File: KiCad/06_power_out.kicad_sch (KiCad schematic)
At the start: 20 parts, among them J601 Conn_02x03_Odd_Even, J602 Conn_02x03_Odd_Even

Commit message: Fill BOM table
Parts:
- C601, C602, C603: footprint Capacitor_SMD:C_0805_2012Metric -> Capacitor_SMD:C_0603_1608Metric; Manufacturer Part Number (none) -> CL10A226MP8NUNE; Manufacturer Product Number CL21A226MQQNNNE -> (none)
- S601, S602, S603: Manufacturer (none) -> XKB Connectivity; Manufacturer Part Number (none) -> XKB5858-Z; Manufacturer_Name XKB Connectivity -> (none); Manufacturer_Part_Number XKB5858-Z -> (none)
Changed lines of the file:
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@@
 			)
 		)
-		(property "Footprint" "Capacitor_SMD:C_0805_2012Metric"
+		(property "Footprint" "Capacitor_SMD:C_0603_1608Metric"
 			(at 116.5352 129.54 0)
 			(effects
@@
 			)
 		)
-		(property "Manufacturer Product Number" "CL21A226MQQNNNE"
+		(property "Manufacturer Part Number" "CL10A226MP8NUNE"
 			(at 115.57 125.73 0)
 			(effects
@@
 			)
 		)
-		(property "Manufacturer_Name" "XKB Connectivity"
-			(at 80.01 539.37 0)
-			(effects
-				(font
-					(size 1.27 1.27)
-				)
-				(justify left top)
-				(hide yes)
-			)
-		)
-		(property "Manufacturer_Part_Number" "XKB5858-Z"
-			(at 80.01 639.37 0)
+		(property "Arrow Part Number" ""
+			(at 80.01 939.37 0)
 			(effects
 				(font
@@
 			)
 		)
-		(property "Mouser Part Number" ""
-			(at 80.01 739.37 0)
+		(property "Arrow Price/Stock" ""
+			(at 80.01 1039.37 0)
 			(effects
 				(font
@@
 			)
 		)
-		(property "Mouser Price/Stock" ""
-			(at 80.01 839.37 0)
+		(property "Manufacturer" "XKB Connectivity"
+			(at 53.34 44.45 0)
 			(effects
 				(font
 					(size 1.27 1.27)
 				)
-				(justify left top)
 				(hide yes)
 			)
 		)
-		(property "Arrow Part Number" ""
-			(at 80.01 939.37 0)
+		(property "Manufacturer Part Number" "XKB5858-Z"
+			(at 53.34 44.45 0)
 			(effects
 				(font
 					(size 1.27 1.27)
 				)
-				(justify left top)
-				(hide yes)
-			)
-		)
-		(property "Arrow Price/Stock" ""
-			(at 80.01 1039.37 0)
-			(effects
-				(font
-					(size 1.27 1.27)
-				)
-				(justify left top)
 				(hide yes)
 			)
@@
 			)
 		)
-		(property "Footprint" "Capacitor_SMD:C_0805_2012Metric"
+		(property "Footprint" "Capacitor_SMD:C_0603_1608Metric"
 			(at 112.7252 48.26 0)
 			(effects
@@
 			)
 		)
-		(property "Manufacturer Product Number" "CL21A226MQQNNNE"
+		(property "Manufacturer Part Number" "CL10A226MP8NUNE"
 			(at 111.76 44.45 0)
 			(effects
@@
 			)
 		)
-		(property "Manufacturer_Name" "XKB Connectivity"
-			(at 80.01 618.11 0)
-			(effects
-				(font
-					(size 1.27 1.27)
-				)
-				(justify left top)
-				(hide yes)
-			)
-		)
-		(property "Manufacturer_Part_Number" "XKB5858-Z"
-			(at 80.01 718.11 0)
-			(effects
-				(font
-					(size 1.27 1.27)
-				)
-				(justify left top)
-				(hide yes)
-			)
-		)
-		(property "Mouser Part Number" ""
-			(at 80.01 818.11 0)
+		(property "Arrow Part Number" ""
+			(at 80.01 1018.11 0)
 			(effects
 				(font
@@
 			)
 		)
-		(property "Mouser Price/Stock" ""
-			(at 80.01 918.11 0)
+		(property "Arrow Price/Stock" ""
+			(at 80.01 1118.11 0)
 			(effects
 				(font
@@
 			)
 		)
-		(property "Arrow Part Number" ""
-			(at 80.01 1018.11 0)
+		(property "Manufacturer" "XKB Connectivity"
+			(at 53.34 123.19 0)
 			(effects
 				(font
 					(size 1.27 1.27)
 				)
-				(justify left top)
 				(hide yes)
 			)
 		)
-		(property "Arrow Price/Stock" ""
-			(at 80.01 1118.11 0)
+		(property "Manufacturer Part Number" "XKB5858-Z"
+			(at 53.34 123.19 0)
 			(effects
 				(font
 					(size 1.27 1.27)
 				)
-				(justify left top)
 				(hide yes)
 			)
@@
 			)
 		)
-		(property "Manufacturer_Name" "XKB Connectivity"
-			(at 80.01 577.47 0)
-			(effects
-				(font
-					(size 1.27 1.27)
-				)
-				(justify left top)
-				(hide yes)
-			)
-		)
-		(property "Manufacturer_Part_Number" "XKB5858-Z"
-			(at 80.01 677.47 0)
-			(effects
-				(font
-					(size 1.27 1.27)
-				)
-				(justify left top)
-				(hide yes)
-			)
-		)
-		(property "Mouser Part Number" ""
-			(at 80.01 777.47 0)
+		(property "Arrow Part Number" ""
+			(at 80.01 977.47 0)
 			(effects
 				(font
@@
 			)
 		)
-		(property "Mouser Price/Stock" ""
-			(at 80.01 877.47 0)
+		(property "Arrow Price/Stock" ""
+			(at 80.01 1077.47 0)
 			(effects
 				(font
@@
 			)
 		)
-		(property "Arrow Part Number" ""
-			(at 80.01 977.47 0)
+		(property "Manufacturer" "XKB Connectivity"
+			(at 53.34 82.55 0)
 			(effects
 				(font
 					(size 1.27 1.27)
 				)
-				(justify left top)
 				(hide yes)
 			)
 		)
-		(property "Arrow Price/Stock" ""
-			(at 80.01 1077.47 0)
+		(property "Manufacturer Part Number" "XKB5858-Z"
+			(at 53.34 82.55 0)
 			(effects
 				(font
 					(size 1.27 1.27)
 				)
-				(justify left top)
 				(hide yes)
 			)
@@
 			)
 		)
-		(property "Footprint" "Capacitor_SMD:C_0805_2012Metric"
+		(property "Footprint" "Capacitor_SMD:C_0603_1608Metric"
 			(at 112.7252 86.36 0)
 			(effects
@@
 			)
 		)
-		(property "Manufacturer Product Number" "CL21A226MQQNNNE"
+		(property "Manufacturer Part Number" "CL10A226MP8NUNE"
 			(at 111.76 82.55 0)
 			(effects

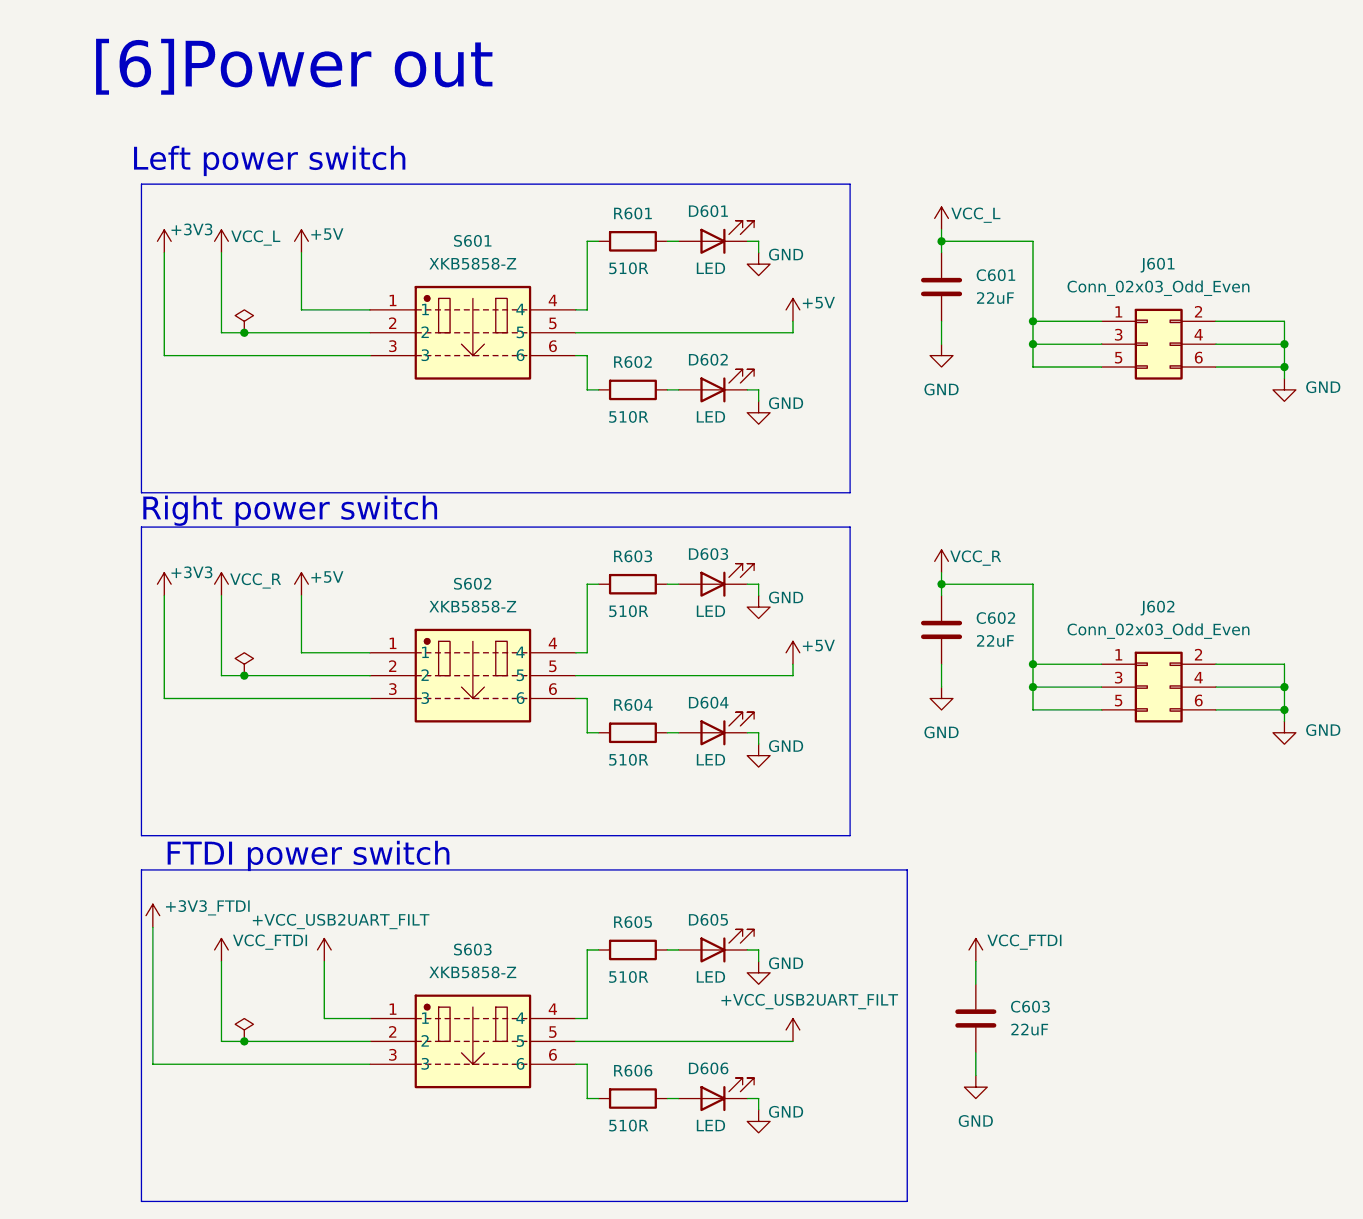
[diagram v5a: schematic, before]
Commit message: Update battery connector
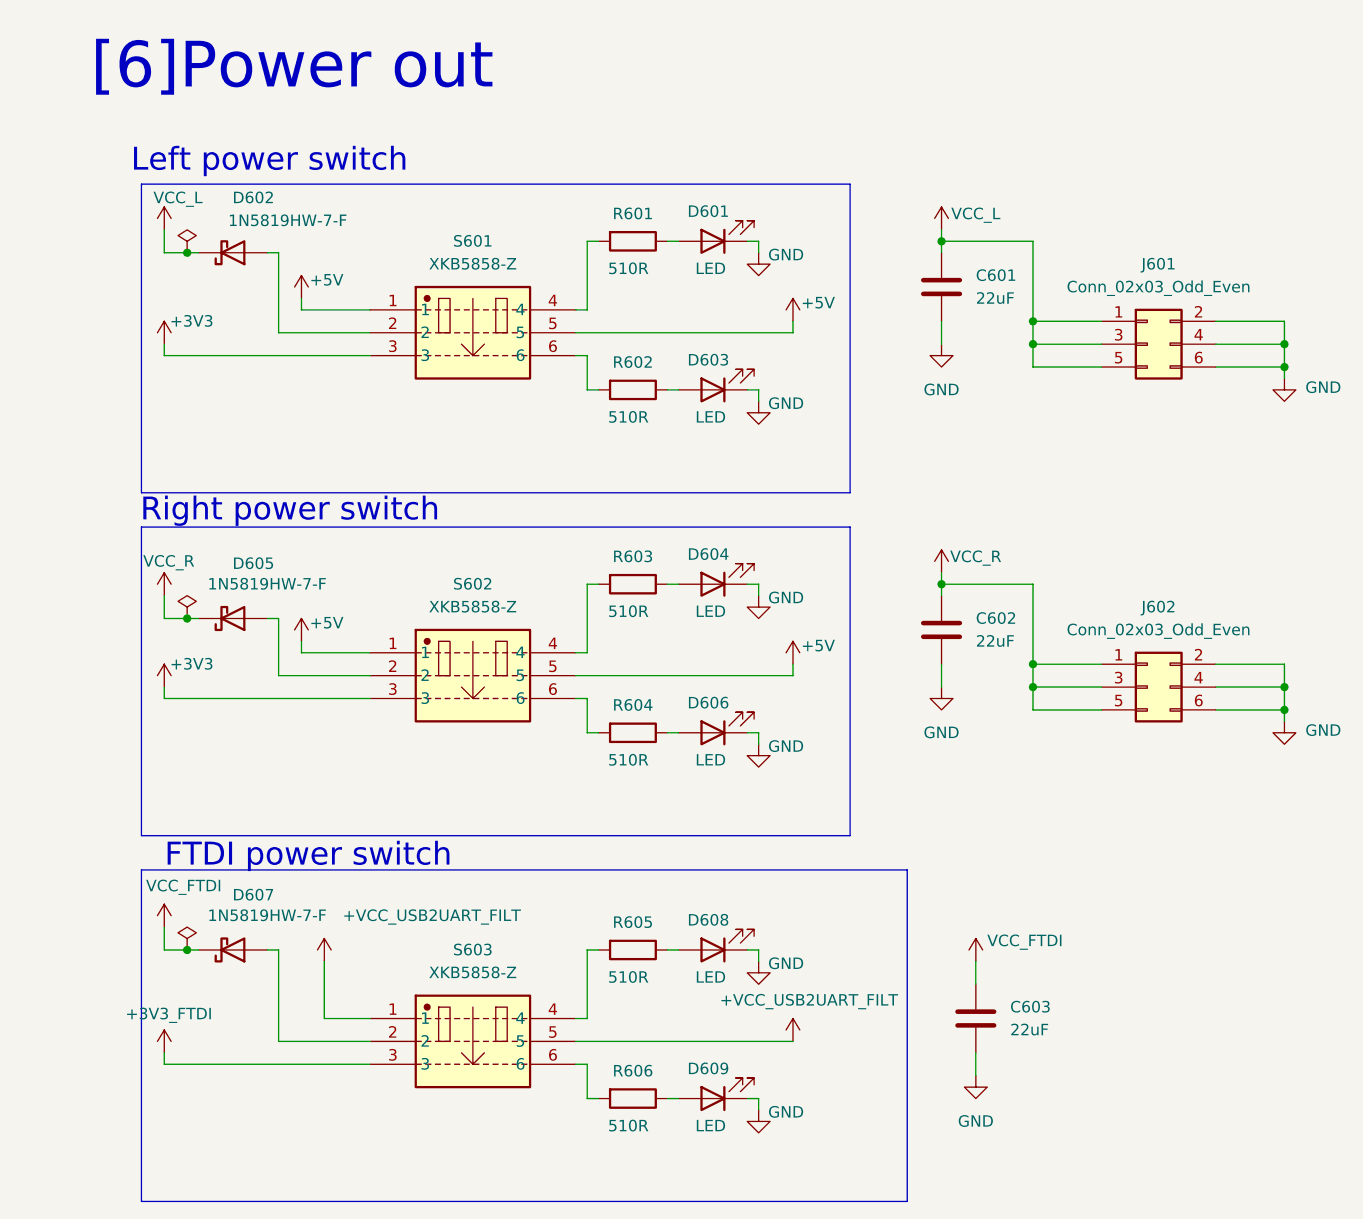
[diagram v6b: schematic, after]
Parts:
- added D602, D605, D607: 1N5819HW-7-F, Diode_SMD:D_SOD-123, symbol Device:D_Schottky
- renumbered D602 to D603, D603 to D604, D604 to D606, D605 to D608, D606 to D609
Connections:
- net VCC_FTDI: now also D607.1 (K); no longer S603.2
- net VCC_L: now also D602.1 (K); no longer S601.2
- net VCC_R: now also D605.1 (K); no longer S602.2
- new net: D605.2 (A), S602.2
- new net: D607.2 (A), S603.2
- new net: D602.2 (A), S601.2

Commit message: BOM updates
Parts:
- R601, R602, R603, R604, R605, R606: Manufacturer UNI-ROYAL(Uniroyal Elec) -> UNI-ROYAL
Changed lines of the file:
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@@
 			)
 		)
-		(property "Manufacturer" "UNI-ROYAL(Uniroyal Elec)"
+		(property "Manufacturer" "UNI-ROYAL"
 			(at 77.47 77.47 0)
 			(effects
@@
 			)
 		)
-		(property "Manufacturer" "UNI-ROYAL(Uniroyal Elec)"
+		(property "Manufacturer" "UNI-ROYAL"
 			(at 77.47 118.11 0)
 			(effects
@@
 			)
 		)
-		(property "Manufacturer" "UNI-ROYAL(Uniroyal Elec)"
+		(property "Manufacturer" "UNI-ROYAL"
 			(at 77.47 39.37 0)
 			(effects
@@
 			)
 		)
-		(property "Manufacturer" "UNI-ROYAL(Uniroyal Elec)"
+		(property "Manufacturer" "UNI-ROYAL"
 			(at 77.47 55.88 0)
 			(effects
@@
 			)
 		)
-		(property "Manufacturer" "UNI-ROYAL(Uniroyal Elec)"
+		(property "Manufacturer" "UNI-ROYAL"
 			(at 77.47 134.62 0)
 			(effects
@@
 			)
 		)
-		(property "Manufacturer" "UNI-ROYAL(Uniroyal Elec)"
+		(property "Manufacturer" "UNI-ROYAL"
 			(at 77.47 93.98 0)
 			(effects
